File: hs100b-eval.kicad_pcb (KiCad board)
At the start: 2 copper layers, 60 x 50 mm, 42 parts, among them IC1 HS-100B, J1 SPKR, J2 MIC, J3 RADIO_DATA, SW1 MUTE_REC, SW2 MUTE_PLAY, SW3 VOL_DN, SW4 VOL_UP

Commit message: Add some silkscreen
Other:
- board text added: "HI"
- board text added: "LO"

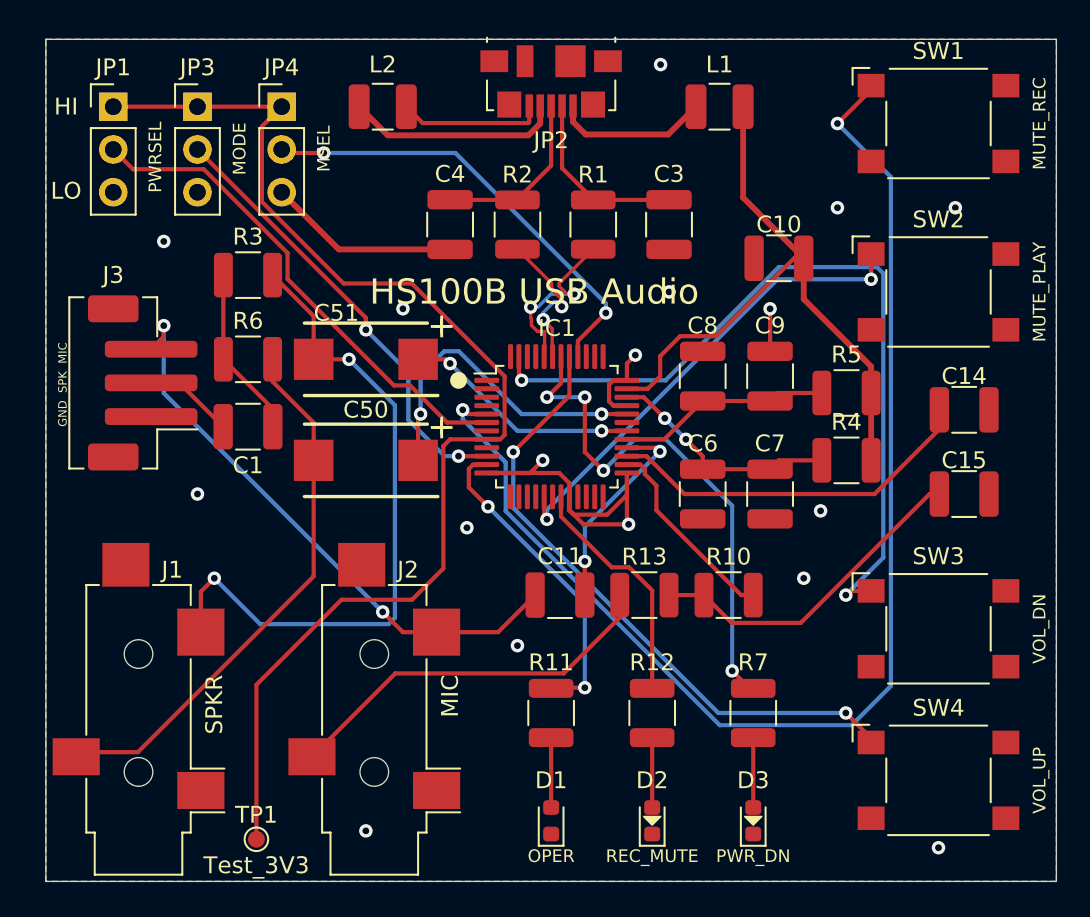
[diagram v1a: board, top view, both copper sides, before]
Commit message: Swap Molex micro USB for CUI
The Molex is nearly impossible to hand solder
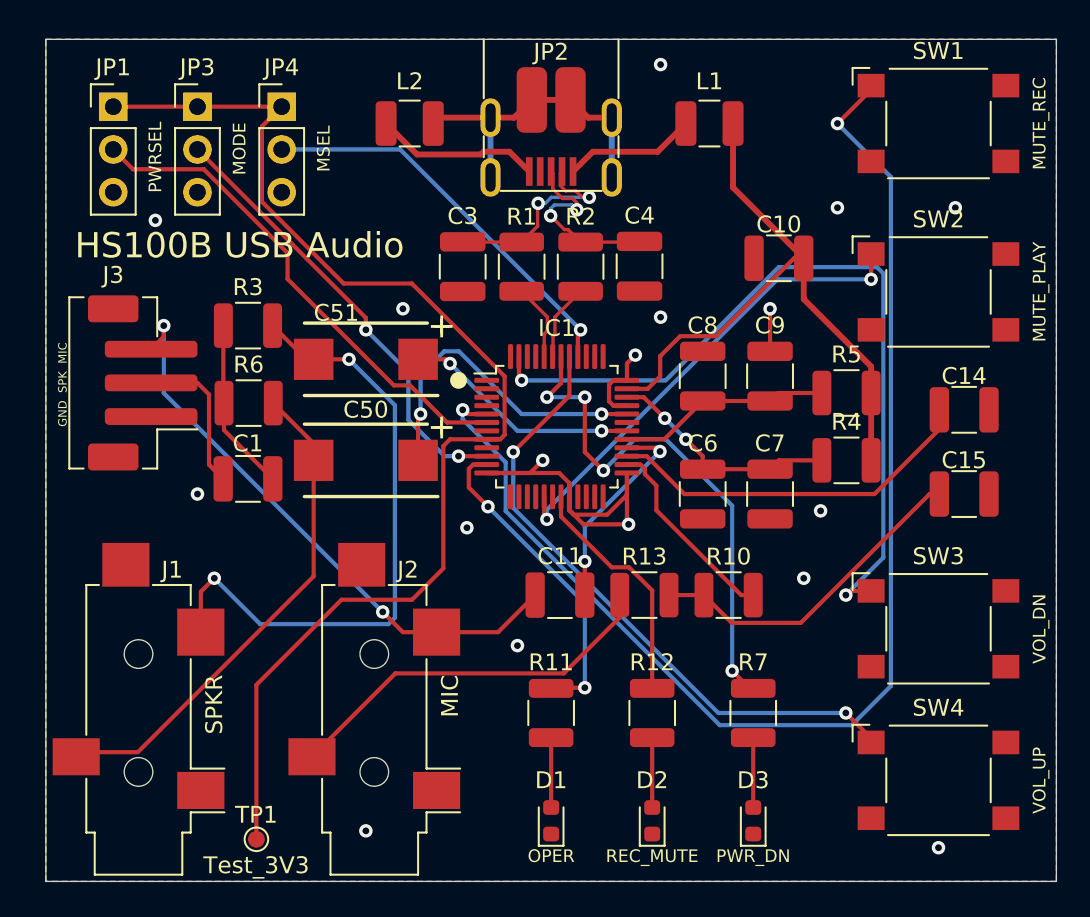
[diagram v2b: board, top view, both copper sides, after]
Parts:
- JP2: value USB_A -> USB_B_Micro; footprint Connector_USB:USB_Micro-B_Molex_47346-0001 -> CUI:UJ2-MIBH-4-SMT
- moved C3 12.5 mm to (154.8, 83.5)
- moved C4 11.5 mm to (165.2, 83.5)
- moved R1 4.93 mm to (158.2, 83.5)
- moved R2 4.51 mm to (161.8, 83.5)
- moved C1 3.10 mm to (142.0, 96.1)
- moved R3 3.00 mm to (142.0, 87.0)
- moved R6 2.60 mm to (142.0, 91.6)
- moved JP2 2.50 mm to (160.0, 70.0), turned to 0 degrees
- moved L2 1.89 mm to (151.6, 75.0)
- moved L1 1.17 mm to (169.4, 75.0)
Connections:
- net Net-(C3-Pad1) renamed /USB-
- net Net-(C4-Pad1) renamed /USB+
- JP2 pad 4: GND -> (no net)
- JP2 pad 5: Net-(JP2-Pad5) -> GND
- JP2 pad 6: (no net) -> Net-(JP2-Pad6)
- L2 pad 2: Net-(JP2-Pad5) -> Net-(JP2-Pad6)
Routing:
- net Net-(JP2-Pad6): track 0.00 -> 18.7 mm
- net GND: track 55.7 -> 41.4 mm
- net Net-(JP2-Pad5): track 8.67 -> 0.00 mm
- net /D-: track 10.6 -> 4.58 mm, vias 2 -> 0
- net /D+: track 8.83 -> 4.56 mm, vias 2 -> 0
- net Net-(C1-Pad2): track 5.35 -> 9.08 mm
- net /MSEL: track 26.9 -> 23.8 mm, vias 2 -> 1
- net /AUDIO_R: track 40.6 -> 37.9 mm
- net /AUDIO_L: track 32.8 -> 30.2 mm
- net /USB-: track 10.8 -> 12.3 mm, vias 0 -> 2
- net Net-(JP2-Pad1): track 9.23 -> 7.88 mm
- net /USB+: track 10.4 -> 11.4 mm, vias 0 -> 2
- net VBUS: track 38.6 -> 37.8 mm
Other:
- net class Signal added: clearance 0.2, trace_width 0.2, via_dia 0.8, via_drill 0.4
- board text added: "HS100B Audio Evaluation Board v2 C. Keller 2021-04-14"
- board text removed: "HI"
- board text removed: "HS100B Audio Evaluation Board v1 C. Keller 2021-04-05"
- board text removed: "LO"

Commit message: Clean up libraries
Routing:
- net GND: track 41.4 -> 42.2 mm

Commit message: Update BOM
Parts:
- C50, C51: footprint 293D477X9010E2TE3:CAPPM7343X430N -> Vishay:CAPPM7343X430N
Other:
- board text removed: "+"

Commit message: Add CC-BY-4.0 license
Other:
- board text added: "HS100B Audio Evaluation Board v2 C. Keller 2021-04-14 https://github.com/k0swe/hs100b-eval"
- board text removed: "HS100B Audio Evaluation Board v2 C. Keller 2021-04-14"

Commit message: Add CUI USB 3D model
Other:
- board text added: "HS100B Audio Evaluation Board v2 C. Keller 2021-04-14"
- board text removed: "HS100B Audio Evaluation Board v2 C. Keller 2021-04-14 https://github.com/k0swe/hs100b-eval"
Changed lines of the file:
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@@
     (rev 2)
     (company "Chris Keller")
-    (comment 1 "Licensed under Creative Commons CC-BY-4.0")
   )
   (layers
@@
     (add_net /USB-)
   )
+  (module CUI:UJ2-MIBH-4-SMT (layer F.Cu)
+    (at 160 70)
+    (fp_text reference JP2 (at 0 0.75) (layer F.SilkS)
+      (effects (font (size 1 1) (thickness 0.15)))
+    )
+    (fp_text value USB_B_Micro (at 0 2.25) (layer F.Fab)
+      (effects (font (size 1 1) (thickness 0.15)))
+    )
+    (fp_text user "PCB Edge" (at 0 -0.75) (layer Dwgs.User)
+      (effects (font (size 1 1) (thickness 0.15)))
+    )
+    (fp_line (start -2 7.45) (end -2 8.8) (layer F.Fab) (width 0.12))
+    (fp_line (start 2 7.45) (end -2 7.45) (layer F.Fab) (width 0.12))
+    (fp_line (start 2 8.8) (end 2 7.45) (layer F.Fab) (width 0.12))
+    (fp_line (start 2 8.8) (end 3.75 8.8) (layer F.Fab) (width 0.12))
+    (fp_line (start -4.5 -3.5) (end -4.5 10) (layer F.CrtYd) (width 0.12))
+    (fp_line (start 4.5 -3.5) (end -4.5 -3.5) (layer F.CrtYd) (width 0.12))
+    (fp_line (start 4.5 10) (end 4.5 -3.5) (layer F.CrtYd) (width 0.12))
+    (fp_line (start -4.5 10) (end 4.5 10) (layer F.CrtYd) (width 0.12))
+    (fp_line (start -4 3.5) (end -4 0) (layer F.SilkS) (width 0.12))
+    (fp_line (start -4 7) (end -4 5.75) (layer F.SilkS) (width 0.12))
+    (fp_line (start 4 3.5) (end 4 0) (layer F.SilkS) (width 0.12))
+    (fp_line (start 4 7) (end 4 5.75) (layer F.SilkS) (width 0.12))
+    (fp_line (start -3 9) (end 3 9) (layer F.SilkS) (width 0.12))
+    (fp_line (start 3.75 -3) (end 3.75 8.8) (layer F.Fab) (width 0.12))
+    (fp_line (start -3.75 -3) (end -3.75 8.8) (layer F.Fab) (width 0.12))
+    (fp_line (start -3.75 8.8) (end -2 8.8) (layer F.Fab) (width 0.12))
+    (fp_line (start -3.75 -3) (end 3.75 -3) (layer F.Fab) (width 0.12))
+    (fp_line (start -3.5 0) (end 3.5 0) (layer Dwgs.User) (width 0.12))
+    (pad 6 smd roundrect (at -1.15 3.6) (size 1.8 3.9) (layers F.Cu F.Paste F.Mask) (roundrect_rratio 0.25)
+      (net 34 "Net-(JP2-Pad6)"))
+    (pad 6 smd roundrect (at 1.15 3.6) (size 1.8 3.9) (layers F.Cu F.Paste F.Mask) (roundrect_rratio 0.25)
+      (net 34 "Net-(JP2-Pad6)"))
+    (pad 5 smd rect (at -1.3 7.85) (size 0.4 1.7) (layers F.Cu F.Paste F.Mask)
+      (net 3 GND))
+    (pad 4 smd rect (at -0.65 7.85) (size 0.4 1.7) (layers F.Cu F.Paste F.Mask))
+    (pad 2 smd rect (at 0.65 7.85) (size 0.4 1.7) (layers F.Cu F.Paste F.Mask)
+      (net 35 /USB-))
+    (pad 3 smd rect (at 0 7.85) (size 0.4 1.7) (layers F.Cu F.Paste F.Mask)
+      (net 36 /USB+))
+    (pad 1 smd rect (at 1.3 7.85) (size 0.4 1.7) (layers F.Cu F.Paste F.Mask)
+      (net 32 "Net-(JP2-Pad1)"))
+    (pad 6 thru_hole oval (at -3.6 4.65) (size 1.2 2.3) (drill oval 0.6 1.7) (layers *.Cu *.Mask)
+      (net 34 "Net-(JP2-Pad6)"))
+    (pad 6 thru_hole oval (at -3.6 8.2) (size 1.2 2.3) (drill oval 0.6 1.7) (layers *.Cu *.Mask)
+      (net 34 "Net-(JP2-Pad6)"))
+    (pad 6 thru_hole oval (at 3.6 8.2) (size 1.2 2.3) (drill oval 0.6 1.7) (layers *.Cu *.Mask)
+      (net 34 "Net-(JP2-Pad6)"))
+    (pad 6 thru_hole oval (at 3.6 4.65) (size 1.2 2.3) (drill oval 0.6 1.7) (layers *.Cu *.Mask)
+      (net 34 "Net-(JP2-Pad6)"))
+    (model ${KIPRJMOD}/Libraries/CUI/CUI_DEVICES_UJ2-MIBH-4-SMT.step
+      (offset (xyz 2 -8.75 2.5))
+      (scale (xyz 1 1 1))
+      (rotate (xyz 0 0 90))
+    )
+  )
   (module Button_Switch_SMD:SW_SPST_Omron_B3FS-100xP (layer F.Cu)
     (at 183 114)
@@
       (rotate (xyz -90 0 -90))
     )
-  )
-  (module CUI:UJ2-MIBH-4-SMT (layer F.Cu)
-    (at 160 70)
-    (fp_text reference JP2 (at 0 0.75) (layer F.SilkS)
-      (effects (font (size 1 1) (thickness 0.15)))
-    )
-    (fp_text value USB_B_Micro (at 0 2.25) (layer F.Fab)
-      (effects (font (size 1 1) (thickness 0.15)))
-    )
-    (fp_line (start -2 7.45) (end -2 8.8) (layer F.Fab) (width 0.12))
-    (fp_line (start 2 7.45) (end -2 7.45) (layer F.Fab) (width 0.12))
-    (fp_line (start 2 8.8) (end 2 7.45) (layer F.Fab) (width 0.12))
-    (fp_line (start 2 8.8) (end 3.75 8.8) (layer F.Fab) (width 0.12))
-    (fp_line (start -4.5 -3.5) (end -4.5 10) (layer F.CrtYd) (width 0.12))
-    (fp_line (start 4.5 -3.5) (end -4.5 -3.5) (layer F.CrtYd) (width 0.12))
-    (fp_line (start 4.5 10) (end 4.5 -3.5) (layer F.CrtYd) (width 0.12))
-    (fp_line (start -4.5 10) (end 4.5 10) (layer F.CrtYd) (width 0.12))
-    (fp_line (start -4 3.5) (end -4 0) (layer F.SilkS) (width 0.12))
-    (fp_line (start -4 7) (end -4 5.75) (layer F.SilkS) (width 0.12))
-    (fp_line (start 4 3.5) (end 4 0) (layer F.SilkS) (width 0.12))
-    (fp_line (start 4 7) (end 4 5.75) (layer F.SilkS) (width 0.12))
-    (fp_line (start -3 9) (end 3 9) (layer F.SilkS) (width 0.12))
-    (fp_line (start 3.75 -3) (end 3.75 8.8) (layer F.Fab) (width 0.12))
-    (fp_line (start -3.75 -3) (end -3.75 8.8) (layer F.Fab) (width 0.12))
-    (fp_line (start -3.75 8.8) (end -2 8.8) (layer F.Fab) (width 0.12))
-    (fp_line (start -3.75 -3) (end 3.75 -3) (layer F.Fab) (width 0.12))
-    (fp_line (start -3.5 0) (end 3.5 0) (layer Dwgs.User) (width 0.12))
-    (fp_text user "PCB Edge" (at 0 -0.75) (layer Dwgs.User)
-      (effects (font (size 1 1) (thickness 0.15)))
-    )
-    (pad 6 smd roundrect (at -1.15 3.6) (size 1.8 3.9) (layers F.Cu F.Paste F.Mask) (roundrect_rratio 0.25)
-      (net 34 "Net-(JP2-Pad6)"))
-    (pad 6 smd roundrect (at 1.15 3.6) (size 1.8 3.9) (layers F.Cu F.Paste F.Mask) (roundrect_rratio 0.25)
-      (net 34 "Net-(JP2-Pad6)"))
-    (pad 5 smd rect (at -1.3 7.85) (size 0.4 1.7) (layers F.Cu F.Paste F.Mask)
-      (net 3 GND))
-    (pad 4 smd rect (at -0.65 7.85) (size 0.4 1.7) (layers F.Cu F.Paste F.Mask))
-    (pad 2 smd rect (at 0.65 7.85) (size 0.4 1.7) (layers F.Cu F.Paste F.Mask)
-      (net 35 /USB-))
-    (pad 3 smd rect (at 0 7.85) (size 0.4 1.7) (layers F.Cu F.Paste F.Mask)
-      (net 36 /USB+))
-    (pad 1 smd rect (at 1.3 7.85) (size 0.4 1.7) (layers F.Cu F.Paste F.Mask)
-      (net 32 "Net-(JP2-Pad1)"))
-    (pad 6 thru_hole oval (at -3.6 4.65) (size 1.2 2.3) (drill oval 0.6 1.7) (layers *.Cu *.Mask)
-      (net 34 "Net-(JP2-Pad6)"))
-    (pad 6 thru_hole oval (at -3.6 8.2) (size 1.2 2.3) (drill oval 0.6 1.7) (layers *.Cu *.Mask)
-      (net 34 "Net-(JP2-Pad6)"))
-    (pad 6 thru_hole oval (at 3.6 8.2) (size 1.2 2.3) (drill oval 0.6 1.7) (layers *.Cu *.Mask)
-      (net 34 "Net-(JP2-Pad6)"))
-    (pad 6 thru_hole oval (at 3.6 4.65) (size 1.2 2.3) (drill oval 0.6 1.7) (layers *.Cu *.Mask)
-      (net 34 "Net-(JP2-Pad6)"))
   )
   (module Package_QFP:LQFP-48_7x7mm_P0.5mm (layer F.Cu)
@@
     (effects (font (size 1.5 1.5) (thickness 0.3)))
   )
-  (gr_text "HS100B Audio\nEvaluation Board v2\nC. Keller 2021-04-14\nhttps://github.com/k0swe/hs100b-eval" (at 162 87.5) (layer B.SilkS)
+  (gr_text "HS100B Audio\nEvaluation Board v2\nC. Keller 2021-04-14" (at 175 81) (layer B.SilkS)
     (effects (font (size 1.5 1.5) (thickness 0.3)) (justify mirror))
   )
